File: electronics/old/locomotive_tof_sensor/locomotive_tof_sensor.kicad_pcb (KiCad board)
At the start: 2 copper layers, 10 x 6 mm, 7 parts, among them J1 TOF, J2 INT, U1 VL6180X

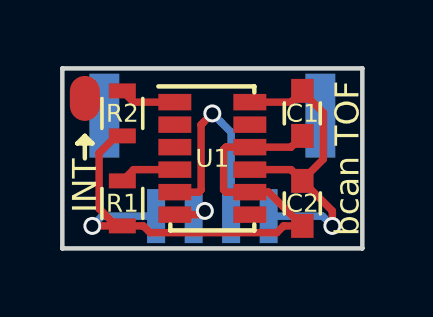
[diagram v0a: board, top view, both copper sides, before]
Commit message: electronics: Rearrange folder structure
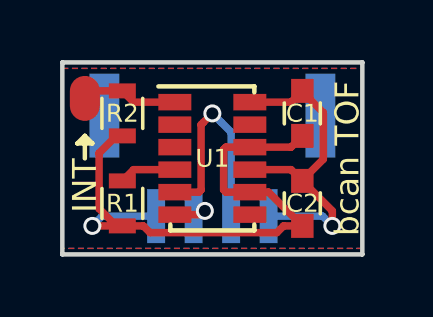
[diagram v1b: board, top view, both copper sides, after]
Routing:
- net /INT: track 1.91 -> 3.26 mm
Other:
- board size 10 x 6 mm -> 10 x 6.4 mm
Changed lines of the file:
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@@
     (links 15)
     (no_connects 0)
-    (area 144.924999 96.924999 155.075001 103.075001)
+    (area 144.407143 94.7 155.575 104.575)
     (thickness 0.8)
     (drawings 12)
-    (tracks 55)
+    (tracks 57)
     (zones 0)
     (modules 7)
@@
     (visible_elements FFFFFF7F)
     (pcbplotparams
-      (layerselection 0x00030_80000001)
-      (usegerberextensions false)
+      (layerselection 0x010f0_80000001)
+      (usegerberextensions true)
       (excludeedgelayer true)
       (linewidth 0.100000)
@@
       (outputformat 1)
       (mirror false)
-      (drillshape 1)
+      (drillshape 0)
       (scaleselection 1)
-      (outputdirectory images))
+      (outputdirectory gerbers))
   )
   (net 0 "")
@@
     (effects (font (size 0.8 0.8) (thickness 0.15)) (justify right))
   )
-  (gr_line (start 145 103) (end 145 97) (layer Edge.Cuts) (width 0.15))
-  (gr_line (start 155 103) (end 145 103) (layer Edge.Cuts) (width 0.15))
-  (gr_line (start 155 97) (end 155 103) (layer Edge.Cuts) (width 0.15))
-  (gr_line (start 145 97) (end 155 97) (layer Edge.Cuts) (width 0.15))
+  (gr_line (start 145 103.2) (end 145 96.8) (layer Edge.Cuts) (width 0.15))
+  (gr_line (start 155 103.2) (end 145 103.2) (layer Edge.Cuts) (width 0.15))
+  (gr_line (start 155 96.8) (end 155 103.2) (layer Edge.Cuts) (width 0.15))
+  (gr_line (start 145 96.8) (end 155 96.8) (layer Edge.Cuts) (width 0.15))
   (segment (start 151.25 101.125) (end 150.45 101.125) (width 0.25) (layer F.Cu) (net 1))
   (segment (start 150.45 101.125) (end 150.374999 101.049999) (width 0.25) (layer F.Cu) (net 1))
@@
   (segment (start 147 100.75) (end 147.375 100.375) (width 0.25) (layer F.Cu) (net 5))
   (segment (start 147.375 100.375) (end 148.75 100.375) (width 0.25) (layer F.Cu) (net 5))
+  (segment (start 147 97.75) (end 146 97.75) (width 0.25) (layer F.Cu) (net 6))
+  (segment (start 146 97.75) (end 145.75 98) (width 0.25) (layer F.Cu) (net 6))
   (segment (start 148.75 98.125) (end 147.375 98.125) (width 0.25) (layer F.Cu) (net 6))
   (segment (start 147.375 98.125) (end 147 97.75) (width 0.25) (layer F.Cu) (net 6))
